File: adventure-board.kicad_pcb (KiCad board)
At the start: 4 copper layers, 90 x 130 mm, 362 parts, among them J1 BreadboardHdr_2x10, J2 Conn_01x05, J4 HY2.0-4P-WT, J5 HY2.0-4P-WT, SW1 SW_MEC_5G, SW2 SW_MEC_5G, SW3 SW_MEC_5G, SW4 SW_MEC_5G, SW5 SW_MEC_5G, SW6 SW_MEC_5G, SW7 BOOTSEL, SW8 RESET, U1 RP2350A, U10 IS31FL3729, U11 IS31FL3729, U2 H5VHD3BC, U3 GT-USB-7010ASV, U4 W25Q64JVSSIQ, U6 PESD5V0U2BT, U7 TPS2065CDBV, U8 PAM8302AASCR, U9 AMS1117-3.3, Y1 12MHz

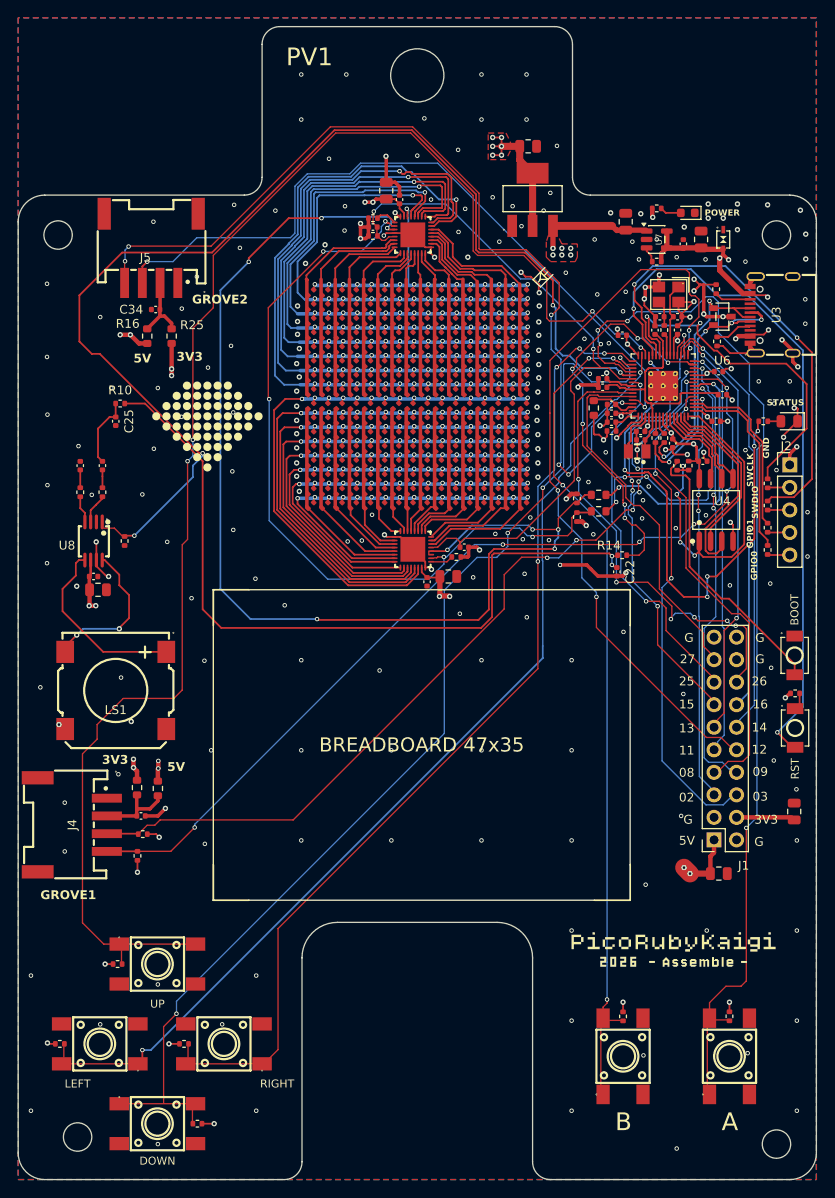
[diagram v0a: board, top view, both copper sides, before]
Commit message: Add V1 (mass production) design data
- Move the two bottom mounting holes to 4.5 mm from the corners, matching the top ones
- Remove the "PV1" silkscreen marking
- Add production/v1 fabrication data and point README to it

Co-Authored-By: Claude Opus 5.5 <noreply@anthropic.com>
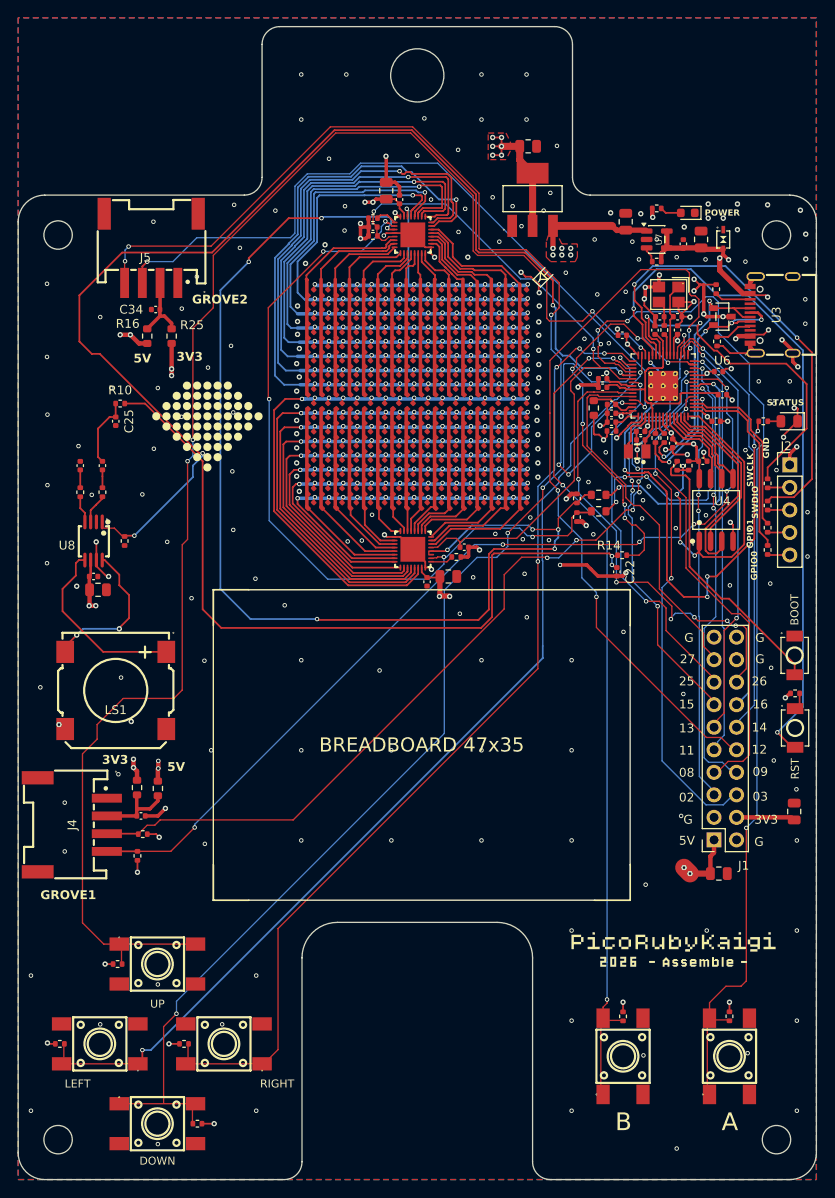
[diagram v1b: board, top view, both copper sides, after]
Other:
- outline, holes or cut-outs redrawn
- board text removed: "PV1"
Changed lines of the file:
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@@
 	)
 	(gr_circle
-		(center 96.7 145.2)
-		(end 98.3 145.2)
+		(center 94.5 145.5)
+		(end 96.1 145.5)
 		(stroke
 			(width 0.1)
@@
 	)
 	(gr_circle
-		(center 175.5 146)
-		(end 177.1 146)
+		(center 175.5 145.5)
+		(end 177.1 145.5)
 		(stroke
 			(width 0.1)
@@
 		)
 	)
-	(gr_text "PV1"
-		(at 120.2 24.6 0)
-		(layer "F.SilkS")
-		(effects
-			(font
-				(size 2 2)
-				(thickness 0.2)
-			)
-			(justify left bottom)
-		)
-	)
